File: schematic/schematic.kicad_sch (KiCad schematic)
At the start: 23 parts, among them U1 ESP32-S3-DevKitC

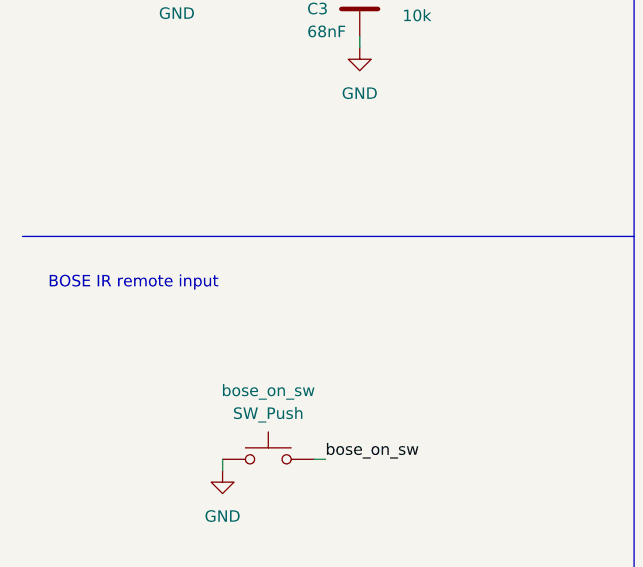
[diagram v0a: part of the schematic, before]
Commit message: Update schematic with note that the IR remote buttons might not be necessary.
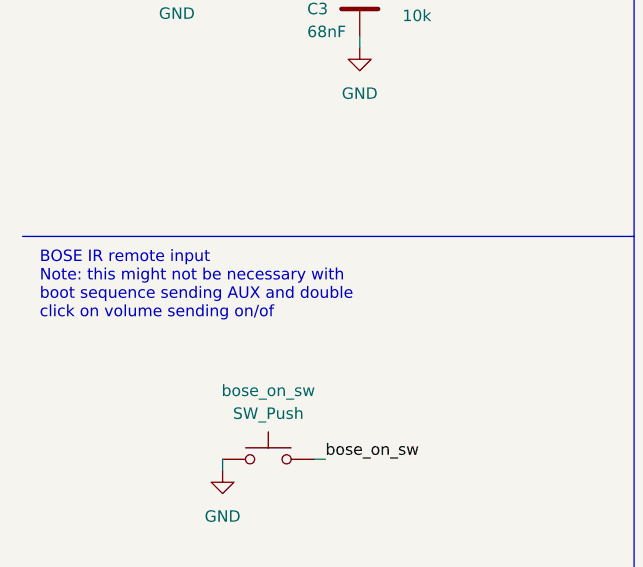
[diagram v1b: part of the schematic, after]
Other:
- note added: "BOSE IR remote input Note: this might not be necessary with boot sequence sending AUX and double click on volume sending on/of"
- note removed: "BOSE IR remote input"
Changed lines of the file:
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@@
 		)
 	)
-	(text "BOSE IR remote input"
+	(text "BOSE IR remote input\nNote: this might not be necessary with\nboot sequence sending AUX and double\nclick on volume sending on/of"
 		(exclude_from_sim no)
-		(at 24.384 135.382 0)
+		(at 13.97 135.636 0)
 		(effects
 			(font
 				(size 1.27 1.27)
 			)
+			(justify left)
 		)
 	)

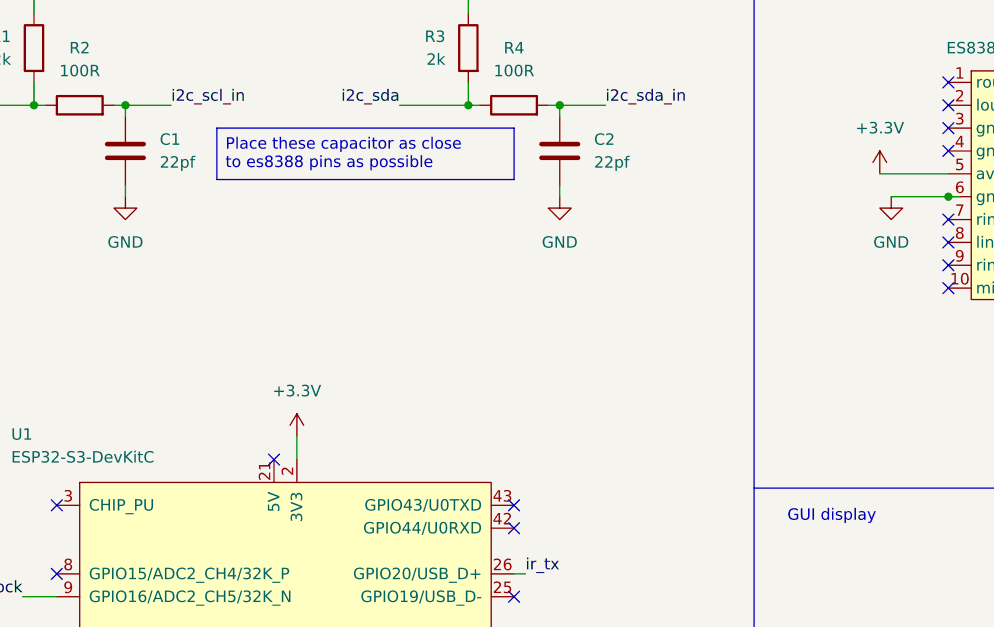
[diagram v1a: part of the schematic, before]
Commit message: add switch to schematic.  added command lines for downloading and uploading json station information.
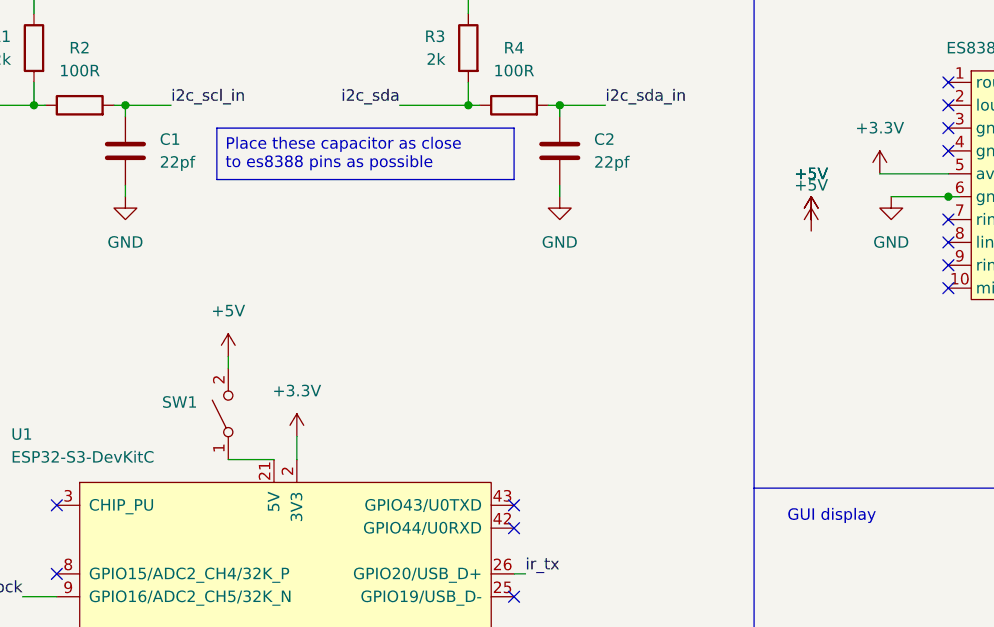
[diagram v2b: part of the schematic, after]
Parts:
- added SW1: SW_SPST, symbol Switch:SW_SPST
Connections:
- net at U1.21 (5V): now also SW1.1 (A)
- new net +5V: SW1.2 (B)
- no-connect marks 25 -> 24
